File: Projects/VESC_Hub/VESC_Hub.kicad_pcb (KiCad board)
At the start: 2 copper layers, 30 parts, among them M1 FE1.1S, P1 USB_OTG_M1, P2 USB_OTG_M2, P3 USB_OTG_M3, P4 USB_DS, P5 USB_OTG_UP, P6 POWER_IN, P7 M1, P8 M2, P9 M3

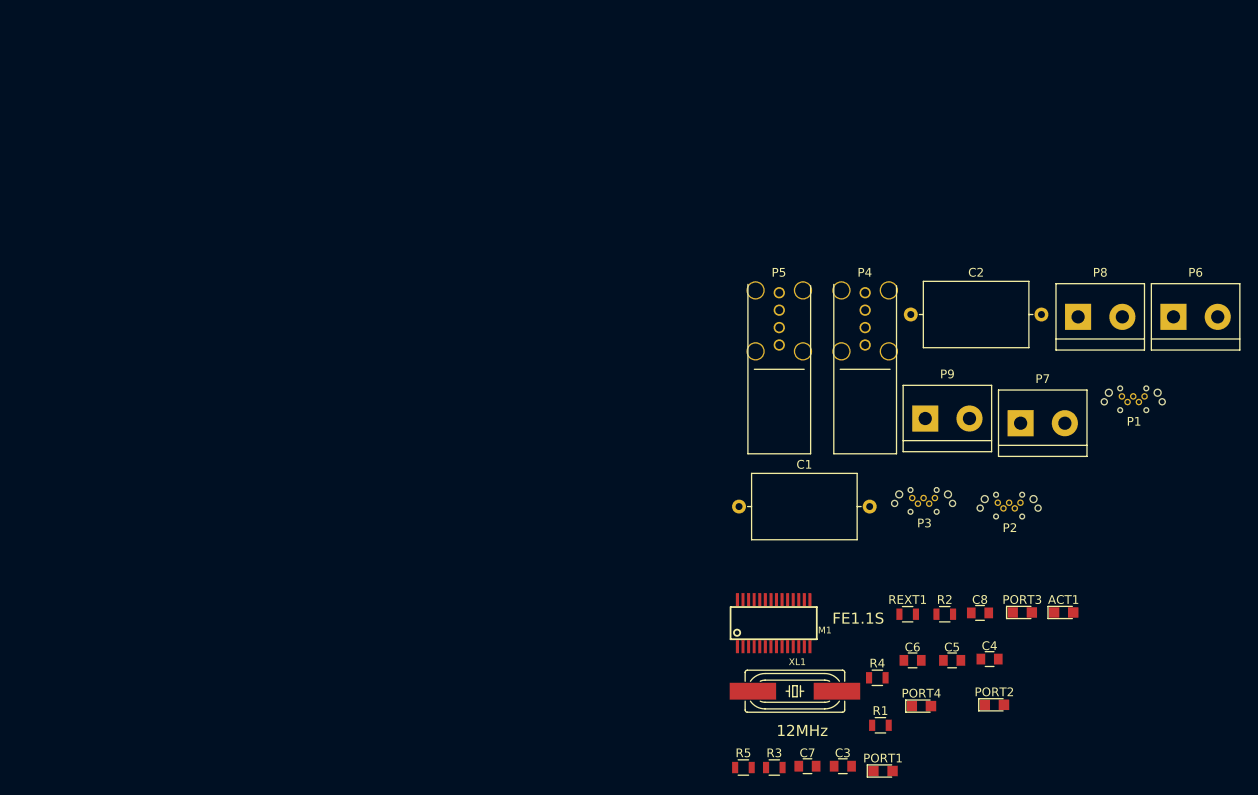
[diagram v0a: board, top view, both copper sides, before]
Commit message: Completed schematics and layout of VESC-X Hub
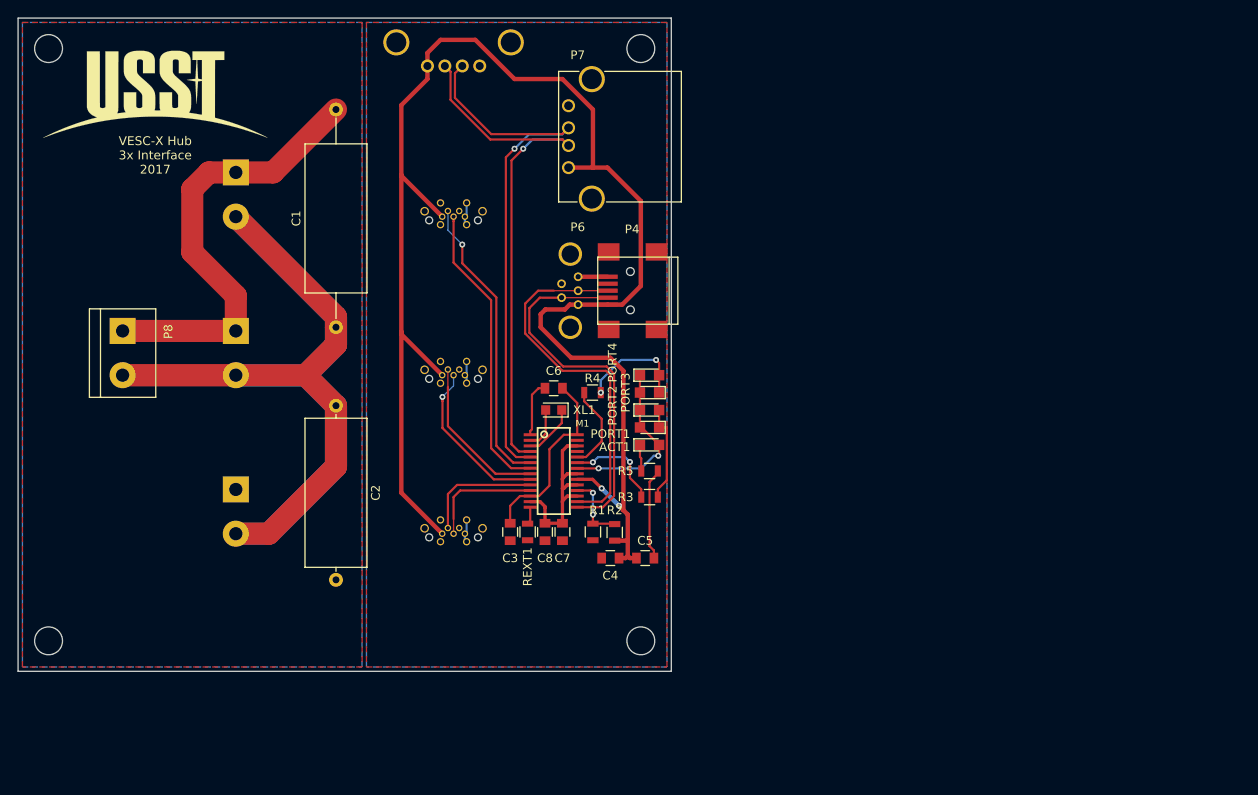
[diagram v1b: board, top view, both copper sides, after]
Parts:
- added G***: LOGO, USST-footprints:USSTLOGO, F.Cu at (65.8, 58.8)
- added G***: LOGO, USST-footprints:OSH_PARK_LOGO_SM, B.Cu at (66.0, 121.5)
- added P6: USB_OTG_UP, USST-footprints:WRCOM_MINI_USB_VERT, F.Cu at (114.3, 81.3)
- added P7: USB_DS, Connect:USB_A, F.Cu at (113.2, 67.2)
- added REF**: MountingHole_3.2mm_M3, Mounting_Holes:MountingHole_3.2mm_M3, F.Cu at (53.5, 53.5)
- added REF**: MountingHole_3.2mm_M3, Mounting_Holes:MountingHole_3.2mm_M3, F.Cu at (121.5, 53.5)
- added REF**: MountingHole_3.2mm_M3, Mounting_Holes:MountingHole_3.2mm_M3, F.Cu at (121.5, 121.5)
- added REF**: MountingHole_3.2mm_M3, Mounting_Holes:MountingHole_3.2mm_M3, F.Cu at (53.5, 121.5)
- C1: footprint Capacitors_ThroughHole:C_Axial_L12.0mm_D7.5mm_P15.00mm_Horizontal -> Capacitors_ThroughHole:C_Axial_L17.0mm_D7.0mm_P25.00mm_Horizontal
- C2: footprint Capacitors_ThroughHole:C_Axial_L12.0mm_D7.5mm_P15.00mm_Horizontal -> Capacitors_ThroughHole:C_Axial_L17.0mm_D7.0mm_P20.00mm_Horizontal
- P1, P2, P3: moved to B.Cu
- P10: renamed from P8; moved to B.Cu
- P11: renamed from P9; moved to B.Cu
- P4: value USB_DS -> USB_OTG_UP; footprint USST-footprints:USB-A-UPRIGHT -> Connect:USB_Mini-B
- P5: value USB_OTG_UP -> USB_DS; footprint USST-footprints:USB-A-UPRIGHT -> USST-footprints:WRCOM_USB_A_VERT; moved to B.Cu
- P9: renamed from P7; moved to B.Cu
- XL1: footprint USST-footprints:HC49UP_SMT_Crystal -> Crystals:Crystal_SMD_2012-2pin_2.0x1.2mm_HandSoldering
- moved P8 120.7 mm to (62.0, 85.9), turned to 270 degrees
- moved P10 98.1 mm to (75.0, 67.7), turned to 270 degrees
- moved P9 90.7 mm to (75.0, 85.9), turned to 270 degrees
- moved P1 79.6 mm to (100.0, 109.2)
- moved P11 79.6 mm to (75.0, 104.1), turned to 270 degrees
- moved C2 66.8 mm to (86.5, 94.5), turned to 270 degrees
- moved P2 65.4 mm to (100.0, 91.0)
- moved P3 62.9 mm to (100.0, 72.8)
- moved PORT2 52.1 mm to (122.5, 95.0)
- moved C6 51.7 mm to (111.5, 92.5), turned to 180 degrees
- moved ACT1 51.3 mm to (122.5, 99.0)
- moved C8 50.8 mm to (110.5, 109.0), turned to 270 degrees
- moved C1 50.6 mm to (86.5, 85.5), turned to 90 degrees
- moved PORT3 49.7 mm to (122.5, 93.0), turned to 180 degrees
- moved PORT4 49.2 mm to (122.5, 91.0)
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- renumbered P6 to P8
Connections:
- M1 pad 10: (no net) -> /USB4_N
- M1 pad 11: (no net) -> /USB4_P
- M1 pad 15: (no net) -> /USBUP_N
- M1 pad 16: (no net) -> /USBUP_P
- M1 pad 4: (no net) -> /USB1_N
- M1 pad 5: (no net) -> /USB1_P
- M1 pad 6: (no net) -> /USB2_N
- M1 pad 7: (no net) -> /USB2_P
- M1 pad 8: (no net) -> /USB3_N
- M1 pad 9: (no net) -> /USB3_P
- P10 pad 1: +24V -> GND
- P10 pad 2: GND -> +24V
- P11 pad 1: +24V -> GND
- P11 pad 2: GND -> +24V
- P8 pad 1: +24V -> GND
- P8 pad 2: GND -> +24V
- P9 pad 1: +24V -> GND
- P9 pad 2: GND -> +24V
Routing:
- net +5V: track 0.00 -> 179.2 mm, vias 0 -> 2
- net +24V: track 0.00 -> 152.1 mm
- net /USB1_P: track 0.00 -> 64.2 mm, vias 0 -> 1
- net /USB1_N: track 0.00 -> 62.8 mm, vias 0 -> 1
- net GND: track 0.00 -> 51.6 mm
- net /USBUP_N: track 0.00 -> 45.1 mm
- net /USBUP_P: track 0.00 -> 43.0 mm
- net /USB2_N: track 0.00 -> 34.0 mm, vias 0 -> 1
- net /USB2_P: track 0.00 -> 33.8 mm
- net GNDD: track 0.00 -> 28.5 mm
- net VDD: track 0.00 -> 23.9 mm
- net Net-(C3-Pad1): track 0.00 -> 21.6 mm
- net Net-(ACT1-Pad2): track 0.00 -> 20.4 mm, vias 0 -> 2
- net /USB3_P: track 0.00 -> 19.1 mm, vias 0 -> 1
- net /USB3_N: track 0.00 -> 18.2 mm
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- added copper zone on B.Cu, net GND
- added copper zone on F.Cu, net GND
- added copper zone on B.Cu, net GNDD
- added copper zone on F.Cu, net GNDD
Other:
- board outline added: 75 x 75 mm
- net class Default: clearance 0.2 -> 0.1524; trace_width 0.25 -> 0.1524; via_dia 0.6 -> 0.6858; via_drill 0.4 -> 0.3302
- rule trace_clearance: 0.2 -> 0.1524
- rule trace_min: 0.2 -> 0.1524
- rule via_min_drill: 0.3 -> 0.3302
- rule via_min_size: 0.4 -> 0.6858
- board text added: "Austin Shirley"
- board text added: "VESC-X Hub 3x Interface 2017"

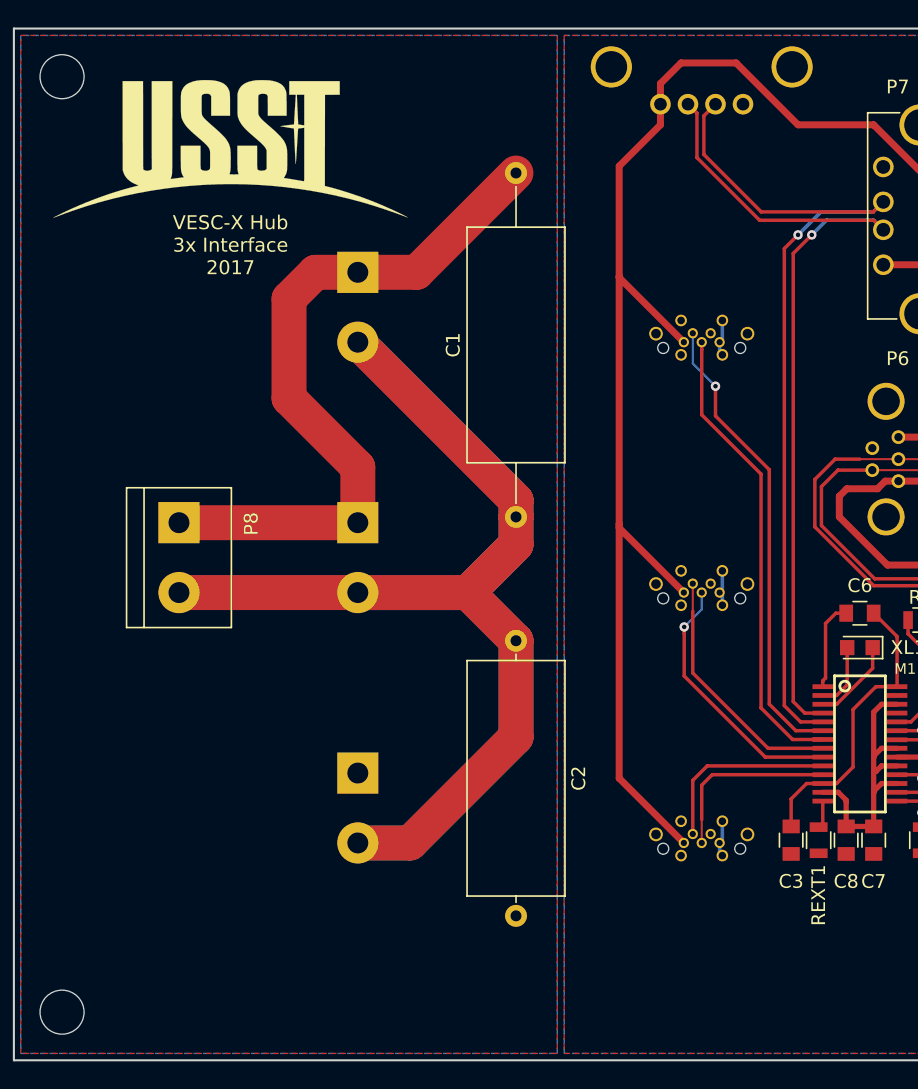
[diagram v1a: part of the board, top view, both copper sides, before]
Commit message: edited hub board to not look like a panelized design, created gerbers
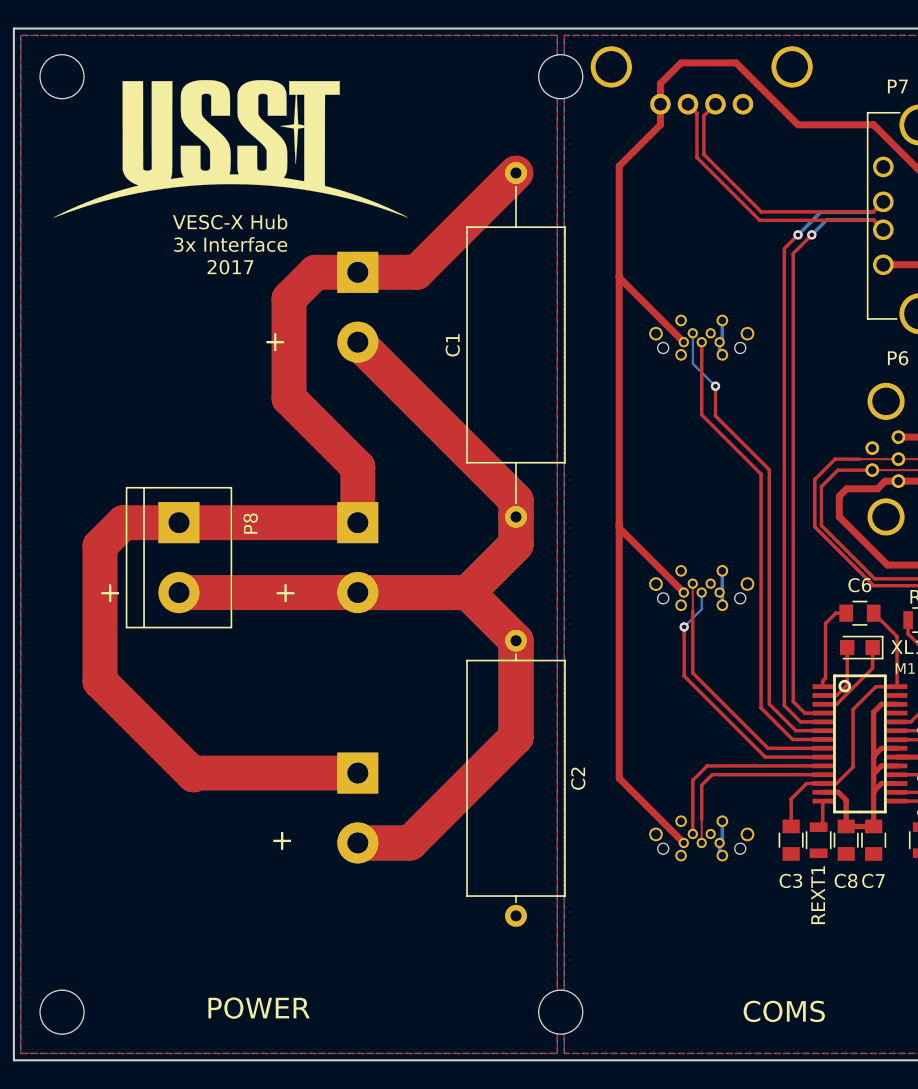
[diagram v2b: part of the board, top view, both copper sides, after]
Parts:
- removed the G*** at (66.0, 121.5)
- added REF**: MountingHole_3.2mm_M3, Mounting_Holes:MountingHole_3.2mm_M3, F.Cu at (89.8, 53.5)
- added REF**: MountingHole_3.2mm_M3, Mounting_Holes:MountingHole_3.2mm_M3, F.Cu at (89.8, 121.5)
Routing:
- net GND: track 51.6 -> 89.5 mm
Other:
- board text added: "+"
- board text added: "COMS"
- board text added: "POWER"
